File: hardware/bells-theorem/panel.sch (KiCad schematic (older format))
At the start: 96 parts, among them J10 D, J11 C, J12 DA, J13 CD, J14 DAB, J15 CDA, J16 A, J17 B, J18 AB, J19 BC, J20 ABC, J21 BCD, J22 left, J23 right, J4 IN, J5 CVA, J6 CVB, J7 CVC, J8 CVD, J9 ABCD, Q1 2N3904, Q10 2N3904, Q11 2N3904, Q12 2N3904, Q13 2N3904, Q2 2N3904, Q3 2N3904, Q4 2N3904, Q5 2N3904, Q6 2N3904, Q7 2N3904, Q8 2N3904, Q9 2N3904

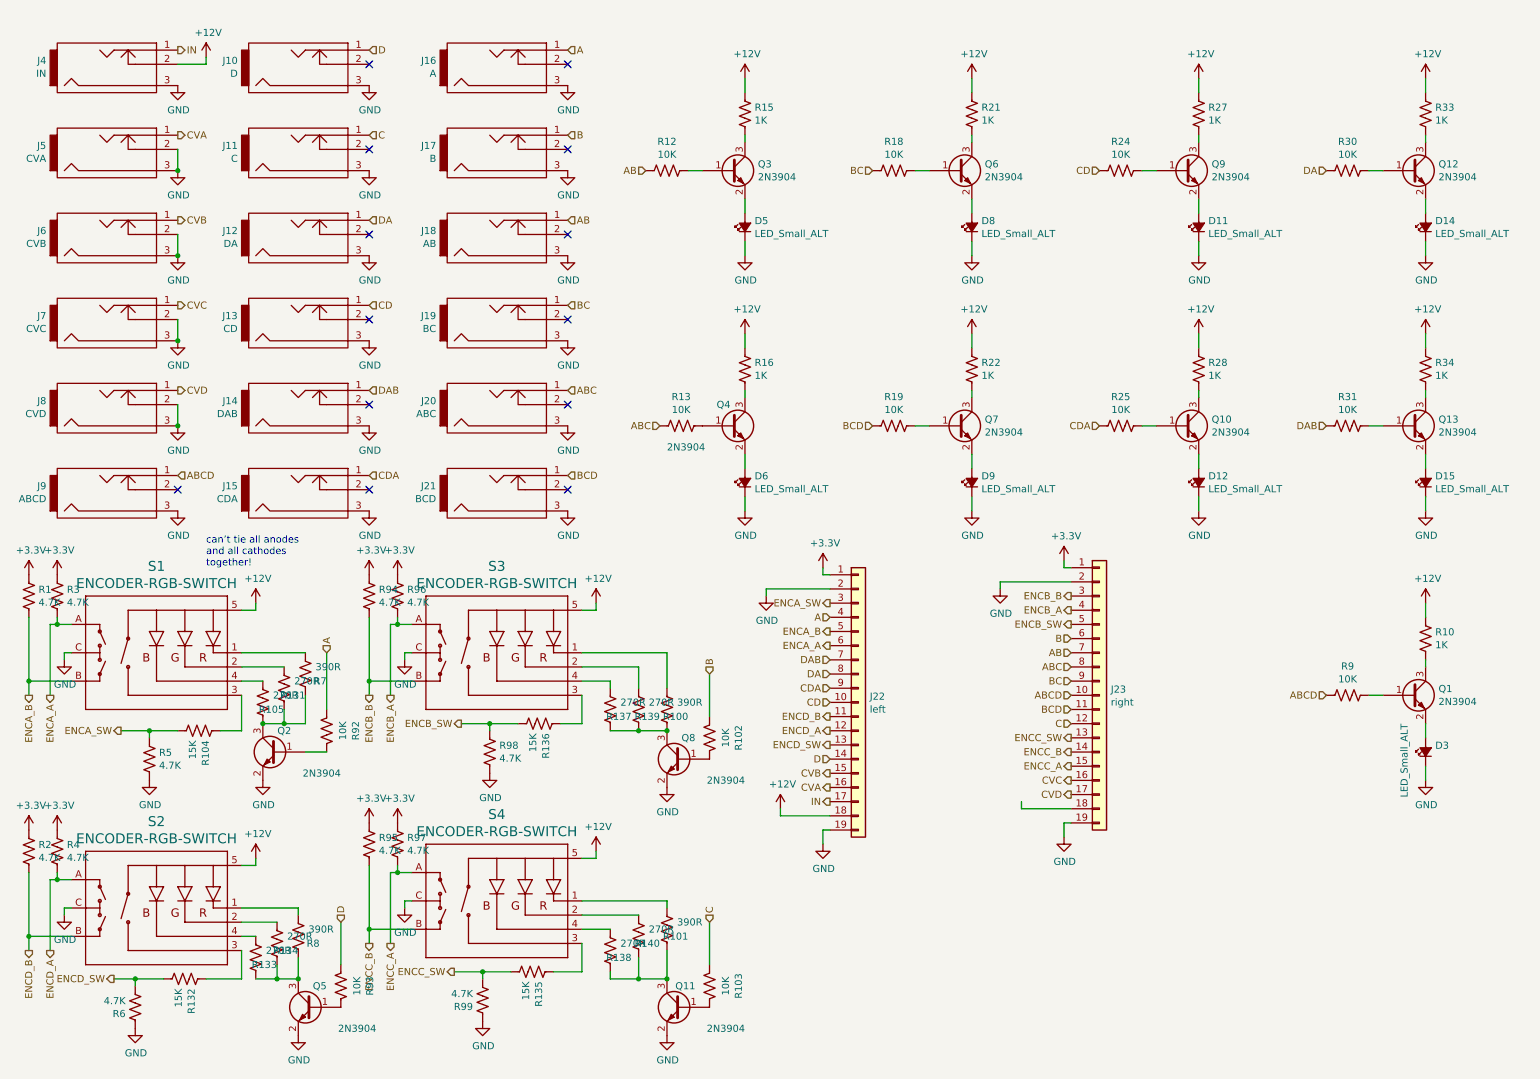
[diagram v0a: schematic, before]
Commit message: version 0.3, update for corrected LED drivers, other tweaks
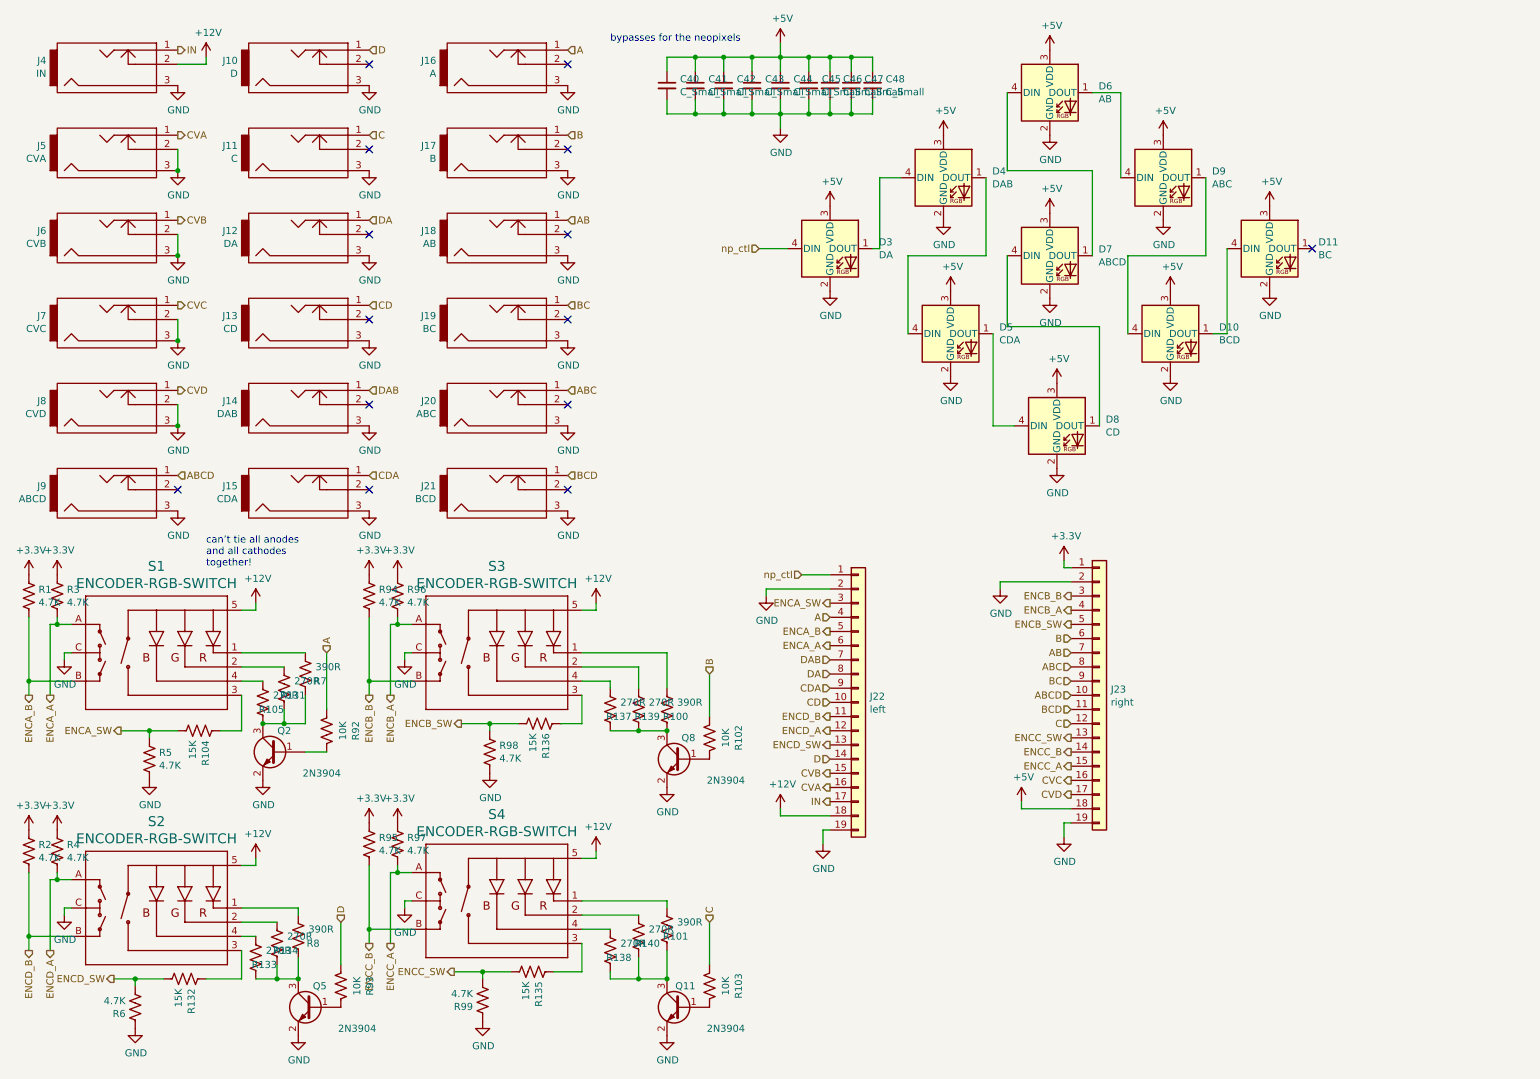
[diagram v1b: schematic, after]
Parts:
- removed D11, D12, D14, D15, D3, D5, D6, D8, D9: LED_Small_ALT, LED_THT:LED_D5.0mm_Clear, symbol device:LED_Small_ALT
- removed Q1, Q10, Q12, Q13, Q3, Q4, Q6, Q7, Q9: 2N3904, Package_TO_SOT_SMD:SOT-23_Handsoldering, symbol device:Q_NPN_BEC
- removed R10, R15, R16, R21, R22, R27, R28, R33, R34: 1K, Resistor_SMD:R_0805_2012Metric_Pad1.15x1.40mm_HandSolder, symbol device:R_US
- removed R12, R13, R18, R19, R24, R25, R30, R31, R9: 10K, Resistor_SMD:R_0805_2012Metric_Pad1.15x1.40mm_HandSolder, symbol device:R_US
- added C40, C41, C42, C43, C44, C45, C46, C47, C48: C_Small, Capacitor_SMD:C_0805_2012Metric_Pad1.15x1.40mm_HandSolder, symbol device:C_Small
- added D10: BCD, LED_THT:LED_D5.0mm-4_RGB_Wide_Pins, symbol LED:NeoPixel_THT
- added D11: BC, LED_THT:LED_D5.0mm-4_RGB_Wide_Pins, symbol LED:NeoPixel_THT
- added D3: DA, LED_THT:LED_D5.0mm-4_RGB_Wide_Pins, symbol LED:NeoPixel_THT
- added D4: DAB, LED_THT:LED_D5.0mm-4_RGB_Wide_Pins, symbol LED:NeoPixel_THT
- added D5: CDA, LED_THT:LED_D5.0mm-4_RGB_Wide_Pins, symbol LED:NeoPixel_THT
- added D6: AB, LED_THT:LED_D5.0mm-4_RGB_Wide_Pins, symbol LED:NeoPixel_THT
- added D7: ABCD, LED_THT:LED_D5.0mm-4_RGB_Wide_Pins, symbol LED:NeoPixel_THT
- added D8: CD, LED_THT:LED_D5.0mm-4_RGB_Wide_Pins, symbol LED:NeoPixel_THT
- added D9: ABC, LED_THT:LED_D5.0mm-4_RGB_Wide_Pins, symbol LED:NeoPixel_THT
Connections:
- net +3V3: no longer J22.1 (Pin_1)
- net GND: now also C40.2, C41.2, C42.2, C43.2, C44.2, C45.2, C46.2, C47.2, C48.2, D10.2 (GND), D11.2 (GND), D3.2 (GND), D4.2 (GND), D5.2 (GND), D6.2 (GND), D7.2 (GND), D8.2 (GND), D9.2 (GND)
- net +5V: now reaches J23.18 (Pin_18)
- net +5V: now also C40.1, C41.1, C42.1, C43.1, C44.1, C45.1, C46.1, C47.1, C48.1, D10.3 (VDD), D11.3 (VDD), D3.3 (VDD), D4.3 (VDD), D5.3 (VDD), D6.3 (VDD), D7.3 (VDD), D8.3 (VDD), D9.3 (VDD)
- new net: D6.1 (DOUT), D9.4 (DIN)
- new net: D6.4 (DIN), D7.1 (DOUT)
- new net: D7.4 (DIN), D8.1 (DOUT)
- new net: D5.1 (DOUT), D8.4 (DIN)
- new net: D4.1 (DOUT), D5.4 (DIN)
- new net: D3.1 (DOUT), D4.4 (DIN)
- new net: D10.4 (DIN), D9.1 (DOUT)
- new net: D10.1 (DOUT), D11.4 (DIN)
- new net np_ctl: D3.4 (DIN), J22.1 (Pin_1)
- no-connect marks 13 -> 14
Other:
- note added: "bypasses for the neopixels"

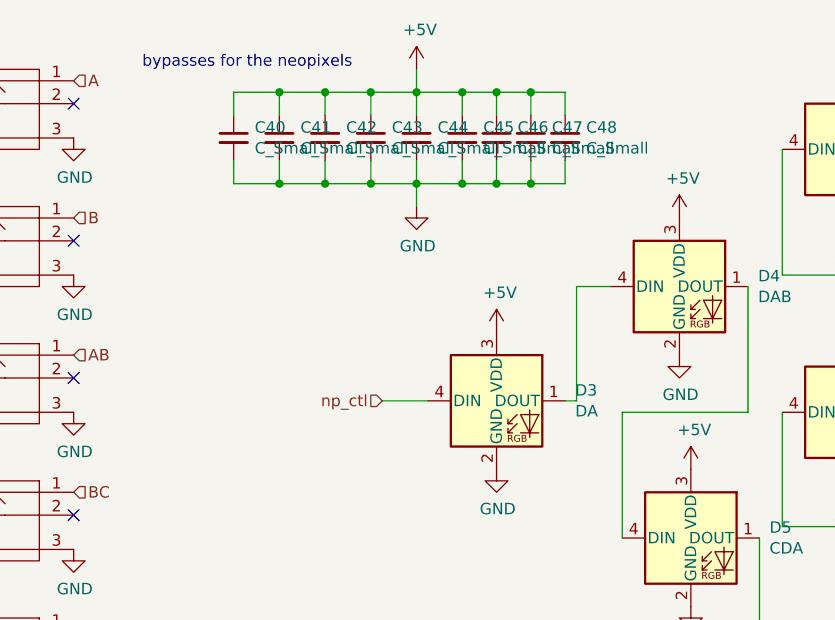
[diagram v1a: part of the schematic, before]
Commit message: updated for NeoPixels
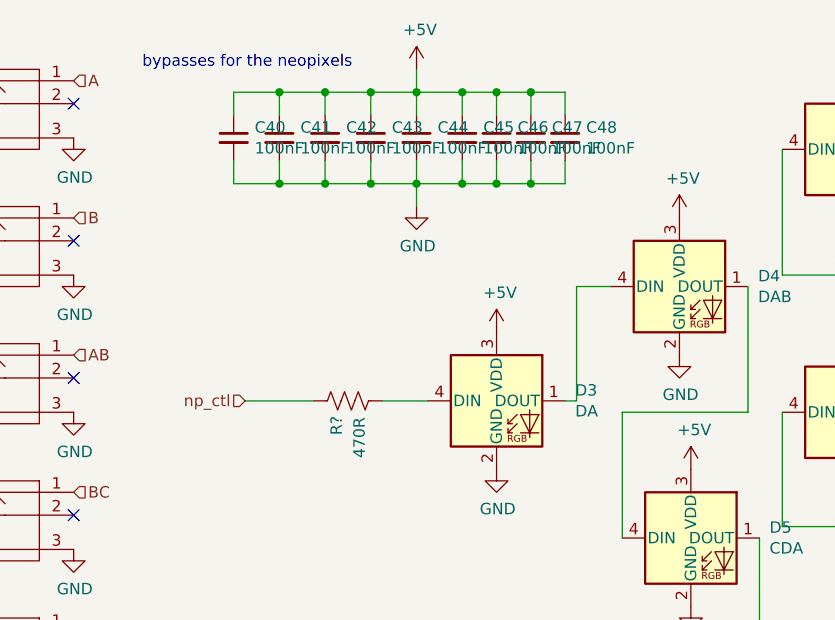
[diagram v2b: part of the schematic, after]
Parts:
- added R?: 470R, Resistor_SMD:R_0805_2012Metric_Pad1.15x1.40mm_HandSolder, symbol device:R_US
- C40, C41, C42, C43, C44, C45, C46, C47, C48: value C_Small -> 100nF
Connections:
- net np_ctl: now also R?.1; no longer D3.4 (DIN)
- new net: D3.4 (DIN), R?.2
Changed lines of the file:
@@
 P 5100 950
 F 0 "C40" H 5192 996 50  0000 L CNN
-F 1 "C_Small" H 5192 905 50  0000 L CNN
+F 1 "100nF" H 5192 905 50  0000 L CNN
 F 2 "Capacitor_SMD:C_0805_2012Metric_Pad1.15x1.40mm_HandSolder" H 5100 950 50  0001 C CNN
 F 3 "~" H 5100 950 50  0001 C CNN
@@
 P 5300 950
 F 0 "C41" H 5392 996 50  0000 L CNN
-F 1 "C_Small" H 5392 905 50  0000 L CNN
+F 1 "100nF" H 5392 905 50  0000 L CNN
 F 2 "Capacitor_SMD:C_0805_2012Metric_Pad1.15x1.40mm_HandSolder" H 5300 950 50  0001 C CNN
 F 3 "~" H 5300 950 50  0001 C CNN
@@
 P 5500 950
 F 0 "C42" H 5592 996 50  0000 L CNN
-F 1 "C_Small" H 5592 905 50  0000 L CNN
+F 1 "100nF" H 5592 905 50  0000 L CNN
 F 2 "Capacitor_SMD:C_0805_2012Metric_Pad1.15x1.40mm_HandSolder" H 5500 950 50  0001 C CNN
 F 3 "~" H 5500 950 50  0001 C CNN
@@
 P 5700 950
 F 0 "C43" H 5792 996 50  0000 L CNN
-F 1 "C_Small" H 5792 905 50  0000 L CNN
+F 1 "100nF" H 5792 905 50  0000 L CNN
 F 2 "Capacitor_SMD:C_0805_2012Metric_Pad1.15x1.40mm_HandSolder" H 5700 950 50  0001 C CNN
 F 3 "~" H 5700 950 50  0001 C CNN
@@
 P 5900 950
 F 0 "C44" H 5992 996 50  0000 L CNN
-F 1 "C_Small" H 5992 905 50  0000 L CNN
+F 1 "100nF" H 5992 905 50  0000 L CNN
 F 2 "Capacitor_SMD:C_0805_2012Metric_Pad1.15x1.40mm_HandSolder" H 5900 950 50  0001 C CNN
 F 3 "~" H 5900 950 50  0001 C CNN
@@
 P 6100 950
 F 0 "C45" H 6192 996 50  0000 L CNN
-F 1 "C_Small" H 6192 905 50  0000 L CNN
+F 1 "100nF" H 6192 905 50  0000 L CNN
 F 2 "Capacitor_SMD:C_0805_2012Metric_Pad1.15x1.40mm_HandSolder" H 6100 950 50  0001 C CNN
 F 3 "~" H 6100 950 50  0001 C CNN
@@
 P 6250 950
 F 0 "C46" H 6342 996 50  0000 L CNN
-F 1 "C_Small" H 6342 905 50  0000 L CNN
+F 1 "100nF" H 6342 905 50  0000 L CNN
 F 2 "Capacitor_SMD:C_0805_2012Metric_Pad1.15x1.40mm_HandSolder" H 6250 950 50  0001 C CNN
 F 3 "~" H 6250 950 50  0001 C CNN
@@
 P 6400 950
 F 0 "C47" H 6492 996 50  0000 L CNN
-F 1 "C_Small" H 6492 905 50  0000 L CNN
+F 1 "100nF" H 6492 905 50  0000 L CNN
 F 2 "Capacitor_SMD:C_0805_2012Metric_Pad1.15x1.40mm_HandSolder" H 6400 950 50  0001 C CNN
 F 3 "~" H 6400 950 50  0001 C CNN
@@
 P 6550 950
 F 0 "C48" H 6642 996 50  0000 L CNN
-F 1 "C_Small" H 6642 905 50  0000 L CNN
+F 1 "100nF" H 6642 905 50  0000 L CNN
 F 2 "Capacitor_SMD:C_0805_2012Metric_Pad1.15x1.40mm_HandSolder" H 6550 950 50  0001 C CNN
 F 3 "~" H 6550 950 50  0001 C CNN
@@
 Text HLabel 6050 4400 0    50   Input ~ 0
 np_ctl
-Text HLabel 5750 2100 0    50   Input ~ 0
+Text HLabel 5150 2100 0    50   Input ~ 0
 np_ctl
 Wire Wire Line
@@
 Wire Wire Line
 	5950 2100 5750 2100
+$Comp
+L device:R_US R?
+U 1 1 6155FA0B
+P 5600 2100
+F 0 "R?" H 5450 2150 50  0000 L CNN
+F 1 "470R" H 5350 2050 50  0000 L CNN
+F 2 "Resistor_SMD:R_0805_2012Metric_Pad1.15x1.40mm_HandSolder" V 5640 2090 50  0001 C CNN
+F 3 "~" H 5600 2100 50  0001 C CNN
+	1    5600 2100
+	0    -1   -1   0
+$EndComp
+Wire Wire Line
+	5150 2100 5450 2100
 $EndSCHEMATC
